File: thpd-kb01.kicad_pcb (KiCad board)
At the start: 2 copper layers, 216 parts, among them SW1 SW_Push, U1 ATmega32U4-AU, Y1 16MHz

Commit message: wip pcb
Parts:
- C1, C2, C3, C4, C5, C6, C7, D1, D10, D100, D11, D12, D13, D14, D15, D16, D17, D18, D19, D2, D20, D21, D22, D23, D24, D25, D26, D27, D28, D29, D3, D30, D31, D32, D33, D34, D35, D36, D37, D38, D39, D4, D40, D41, D42, D43, D44, D45, D46, D47, D48, D49, D5, D50, D51, D52, D53, D54, D55, D56, D57, D58, D59, D6, D60, D61, D62, D63, D64, D65, D66, D67, D68, D69, D7, D70, D71, D72, D73, D74, D75, D76, D77, D78, D79, D8, D80, D81, D82, D83, D84, D85, D86, D87, D88, D89, D9, D90, D91, D92, D93, D94, D95, D96, D97, D98, D99, F1, R1, R2, R3, R4, SW1, U1, USB1, Y1: moved to B.Cu
- moved C2 448.9 mm to (681.0, 19.1)
- moved D89 446.5 mm to (696.9, 39.7), turned to 90 degrees
- moved SW1 445.3 mm to (682.6, 7.94)
- moved R3 441.8 mm to (677.1, 14.3)
- moved U1 438.9 mm to (667.5, 8.73)
- moved R4 435.9 mm to (657.2, 2.38), turned to 270 degrees
- moved C7 434.7 mm to (677.9, -1.59), turned to 180 degrees
- moved C6 431.7 mm to (662.0, -6.35), turned to 270 degrees
- moved C5 430.3 mm to (672.3, -6.35), turned to 90 degrees
- moved Y1 426.9 mm to (666.8, -6.35), turned to 180 degrees
- moved D96 421.3 mm to (677.9, 39.7), turned to 90 degrees
- moved D97 418.5 mm to (677.9, 58.7), turned to 90 degrees
- moved F1 417.6 mm to (631.8, 9.53), turned to 90 degrees
- moved D95 416.4 mm to (689.0, 56.4), turned to 270 degrees
- moved C3 413.1 mm to (656.4, 7.14)
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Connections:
- MX66 pad 1: /keys_matrix/COL11 -> /keys_matrix/COL12

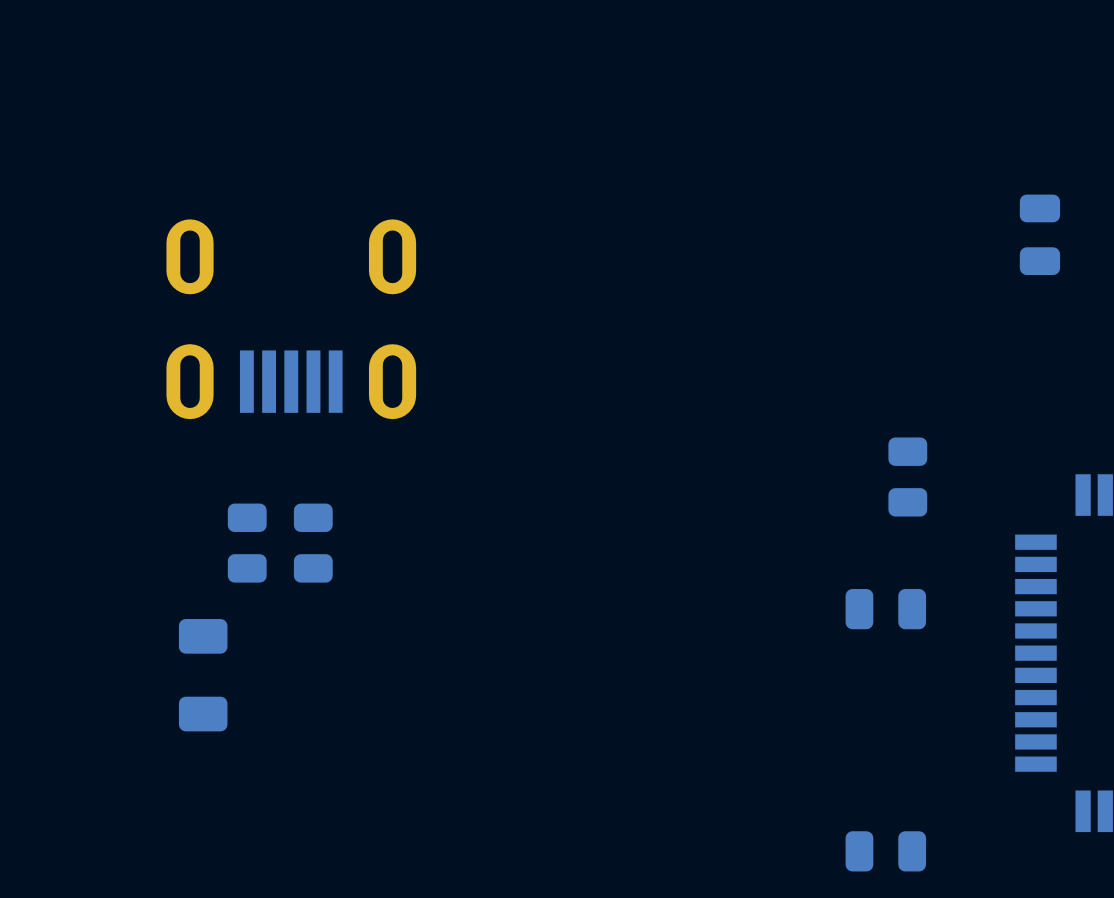
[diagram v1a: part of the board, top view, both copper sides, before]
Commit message: Switch USB B to USB C
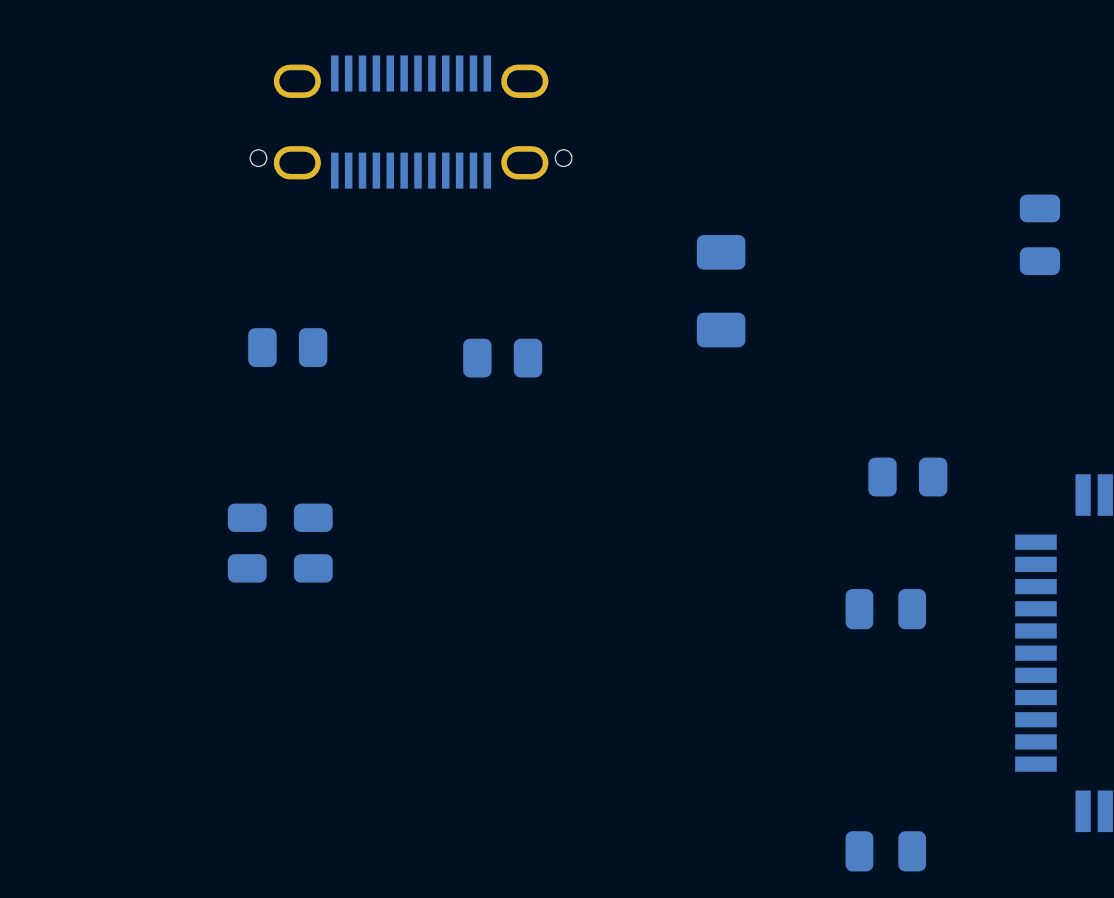
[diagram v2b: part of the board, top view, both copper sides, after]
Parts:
- removed USB1: Molex-0548190589, random-keyboard-parts:Molex-0548190589
- added J1: USB_C_Receptacle_USB2.0, Connector_USB:USB_C_Receptacle_JAE_DX07S024WJ3R400, B.Cu at (639.3, -10.4)
- added R5: 5.1k, Resistor_SMD:R_0805_2012Metric, B.Cu at (634.9, -2.29)
- added R6: 5.1k, Resistor_SMD:R_0805_2012Metric, B.Cu at (642.6, -1.91)
- moved F1 23.2 mm to (650.5, -4.32)
- turned R4 to 0 degrees

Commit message: wip
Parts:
- D1, D10, D100, D11, D12, D13, D14, D15, D16, D17, D18, D19, D2, D20, D21, D22, D23, D24, D25, D26, D27, D28, D29, D3, D30, D31, D32, D33, D34, D35, D36, D37, D38, D39, D4, D40, D41, D42, D43, D44, D45, D46, D47, D48, D49, D5, D50, D51, D52, D53, D54, D55, D56, D57, D58, D59, D6, D60, D61, D62, D63, D64, D65, D66, D67, D68, D69, D7, D70, D71, D72, D73, D74, D75, D76, D77, D78, D79, D8, D80, D81, D82, D83, D84, D85, D86, D87, D88, D89, D9, D90, D91, D92, D93, D94, D95, D96, D97, D98, D99: footprint Diode_SMD:D_SOD-123 -> Diode_SMD:D_SOD-123F
- J1: footprint Connector_USB:USB_C_Receptacle_JAE_DX07S024WJ3R400 -> Connector_USB:USB_C_Receptacle_HRO_TYPE-C-31-M-12
- MX1, MX10, MX11, MX13, MX14, MX15, MX16, MX17, MX19, MX2, MX20, MX21, MX22, MX23, MX24, MX25, MX26, MX27, MX28, MX29, MX30, MX31, MX32, MX33, MX35, MX36, MX37, MX38, MX39, MX40, MX41, MX42, MX43, MX44, MX45, MX46, MX47, MX48, MX49, MX50, MX51, MX52, MX53, MX54, MX55, MX56, MX57, MX58, MX59, MX60, MX61, MX62, MX63, MX64, MX65, MX67, MX68, MX69, MX7, MX70, MX71, MX72, MX75, MX76, MX77, MX78, MX79, MX8, MX80, MX81, MX82, MX83, MX84, MX85, MX86, MX87, MX89, MX9, MX90, MX91, MX92, MX93, MX94, MX96, MX97, MX98, MX99: footprint MX_Alps_Hybrid:MX-1U-NoLED -> Button_Switch_Keyboard:SW_Cherry_MX_1.00u_Plate
- MX100, MX95: footprint MX_Alps_Hybrid:MX-2U-NoLED -> Button_Switch_Keyboard:SW_Cherry_MX_2.00u_Vertical_Plate
- MX12, MX18, MX6: footprint MX_Alps_Hybrid:MX-1.25U-NoLED -> Button_Switch_Keyboard:SW_Cherry_MX_1.25u_Plate
- MX3: footprint MX_Alps_Hybrid:MX-1.5U-NoLED -> Button_Switch_Keyboard:SW_Cherry_MX_1.50u_Plate
- MX34: footprint MX_Alps_Hybrid:MX-6.25U-NoLED -> Button_Switch_Keyboard:SW_Cherry_MX_6.25u_Plate
- MX4, MX66: footprint MX_Alps_Hybrid:MX-1.75U-NoLED -> Button_Switch_Keyboard:SW_Cherry_MX_1.75u_Plate
- MX5: footprint MX_Alps_Hybrid:MX-2.25U-NoLED -> Button_Switch_Keyboard:SW_Cherry_MX_2.25u_Plate
- MX73, MX88: footprint MX_Alps_Hybrid:MX-2U-NoLED -> Button_Switch_Keyboard:SW_Cherry_MX_2.00u_Plate
- MX74: footprint MX_Alps_Hybrid:MX-ISO -> Button_Switch_Keyboard:SW_Cherry_MX_ISOEnter_Plate
- SW1: footprint random-keyboard-parts:SKQG-1155865 -> random-keyboard-parts:SKQGADE010
- moved C6 31.5 mm to (682.6, 17.5)
- moved C5 30.4 mm to (682.6, 22.2), turned to 0 degrees
- moved Y1 28.2 mm to (677.1, 19.8), turned to 270 degrees
- moved J1 22.5 mm to (633.9, 11.4)
- moved R5 22.3 mm to (628.6, 19.2)
- moved F1 20.7 mm to (649.7, 16.3)
- moved R6 19.8 mm to (641.9, 17.9)
- moved C7 16.3 mm to (666.8, 10.3)
- moved R1 16.1 mm to (633.1, 20.8)
- moved R2 16.1 mm to (635.5, 20.8)
- moved SW1 15.7 mm to (696.1, 15.9), turned to 270 degrees
- moved C2 13.5 mm to (670.7, 27.8)
- moved U1 10.3 mm to (666.8, 19.1), turned to 270 degrees
- moved R3 9.66 mm to (686.6, 12.7), turned to 90 degrees
- moved R4 8.59 mm to (662.0, 9.53)
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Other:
- board outline added: 402.4 x 126.2 mm

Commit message: wip
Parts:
- moved D95 15.3 mm to (694.7, 70.6)
- moved D100 12.9 mm to (694.7, 111.3)
- moved D88 7.20 mm to (647.8, 120.6)
- moved SW1 6.40 mm to (692.9, 21.4)
- moved D5 6.32 mm to (341.3, 101.8)
- moved D74 6.22 mm to (593.7, 70.0)
- moved MX91 5.97 mm to (651.0, 59.5)
- moved MX85 5.97 mm to (632.0, 59.5)
- moved C6 5.56 mm to (682.6, 23.0)
- moved R1 5.56 mm to (633.1, 26.4)
- moved R2 5.56 mm to (635.5, 26.4)
- moved R3 5.56 mm to (686.6, 18.3)
- moved R5 5.56 mm to (628.6, 24.7)
- moved C3 5.56 mm to (655.6, 15.9)
- moved C7 5.56 mm to (666.8, 15.9)
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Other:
- board size 402.4 x 126.2 mm -> 390 x 120.6 mm

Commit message: Big changes
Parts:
- removed Y1: 16MHz, Crystal:Crystal_SMD_3225-4Pin_3.2x2.5mm
- added C10: 100nF, Capacitor_SMD:C_0402_1005Metric, F.Cu at (280.1, 71.9)
- added C11: 100nF, Capacitor_SMD:C_0402_1005Metric, F.Cu at (285.2, 67.0)
- added C12: 1uF, Capacitor_SMD:C_0402_1005Metric, F.Cu at (280.1, 69.9)
- added C13: 1uF, Capacitor_SMD:C_0402_1005Metric, F.Cu at (307.0, 42.4)
- added C14: 1uF, Capacitor_SMD:C_0402_1005Metric, F.Cu at (282.0, 67.9)
- added C15: 1uF, Capacitor_SMD:C_0402_1005Metric, F.Cu at (299.8, 53.1)
- added C16: 1uF, Capacitor_SMD:C_0402_1005Metric, F.Cu at (279.1, 67.9)
- added C17: 1uF, Capacitor_SMD:C_0402_1005Metric, F.Cu at (307.0, 40.4)
- added C18: 1uF, Capacitor_SMD:C_0402_1005Metric, F.Cu at (277.2, 71.1)
- added C19: 1uF, Capacitor_SMD:C_0402_1005Metric, F.Cu at (271.5, 70.2)
- added C20: 10nF, Capacitor_SMD:C_0402_1005Metric, F.Cu at (307.0, 48.4)
- added C21: 10nF, Capacitor_SMD:C_0402_1005Metric, F.Cu at (274.3, 71.1)
- added C8: 10nF, Capacitor_SMD:C_0402_1005Metric, F.Cu at (289.2, 64.5)
- added C9: 4.7uF, Capacitor_SMD:C_0402_1005Metric, F.Cu at (307.0, 44.4)
- added D101: D_Small, Diode_SMD:D_SOD-123, B.Cu at (377.8, 191.3)
- added D102: D_Small, Diode_SMD:D_SOD-123, B.Cu at (396.9, 91.3)
- added D103: SK6812, thpd-kb01-custom:LED_SK6812MINI-ER_PLCC4_3.5x2.8mm_P1.8mm, F.Cu at (100.7, 50.7)
- added D104: SK6812, thpd-kb01-custom:LED_SK6812MINI-ER_PLCC4_3.5x2.8mm_P1.8mm, F.Cu at (93.7, 55.7)
- added D105: SK6812, thpd-kb01-custom:LED_SK6812MINI-ER_PLCC4_3.5x2.8mm_P1.8mm, F.Cu at (107.7, 40.6)
- added D106: SK6812, thpd-kb01-custom:LED_SK6812MINI-ER_PLCC4_3.5x2.8mm_P1.8mm, F.Cu at (86.6, 60.8)
- added D107: SK6812, thpd-kb01-custom:LED_SK6812MINI-ER_PLCC4_3.5x2.8mm_P1.8mm, F.Cu at (100.7, 45.6)
- added D108: SK6812, thpd-kb01-custom:LED_SK6812MINI-ER_PLCC4_3.5x2.8mm_P1.8mm, F.Cu at (93.7, 50.7)
- added D109: SK6812, thpd-kb01-custom:LED_SK6812MINI-ER_PLCC4_3.5x2.8mm_P1.8mm, F.Cu at (107.7, 35.5)
- added D110: SK6812, thpd-kb01-custom:LED_SK6812MINI-ER_PLCC4_3.5x2.8mm_P1.8mm, F.Cu at (100.7, 40.6)
- added D111: SK6812, thpd-kb01-custom:LED_SK6812MINI-ER_PLCC4_3.5x2.8mm_P1.8mm, F.Cu at (79.6, 60.8)
- added D112: SK6812, thpd-kb01-custom:LED_SK6812MINI-ER_PLCC4_3.5x2.8mm_P1.8mm, F.Cu at (93.7, 45.6)
- added D113: SK6812, thpd-kb01-custom:LED_SK6812MINI-ER_PLCC4_3.5x2.8mm_P1.8mm, F.Cu at (86.6, 50.7)
- added D114: SK6812, thpd-kb01-custom:LED_SK6812MINI-ER_PLCC4_3.5x2.8mm_P1.8mm, F.Cu at (107.7, 30.5)
- added D115: SK6812, thpd-kb01-custom:LED_SK6812MINI-ER_PLCC4_3.5x2.8mm_P1.8mm, F.Cu at (79.6, 55.7)
- added D116: SK6812, thpd-kb01-custom:LED_SK6812MINI-ER_PLCC4_3.5x2.8mm_P1.8mm, F.Cu at (100.7, 35.5)
- added D117: SK6812, thpd-kb01-custom:LED_SK6812MINI-ER_PLCC4_3.5x2.8mm_P1.8mm, F.Cu at (93.7, 40.6)
- added D118: SK6812, thpd-kb01-custom:LED_SK6812MINI-ER_PLCC4_3.5x2.8mm_P1.8mm, F.Cu at (72.6, 60.8)
- added D119: SK6812, thpd-kb01-custom:LED_SK6812MINI-ER_PLCC4_3.5x2.8mm_P1.8mm, F.Cu at (86.6, 45.6)
- added D120: SK6812, thpd-kb01-custom:LED_SK6812MINI-ER_PLCC4_3.5x2.8mm_P1.8mm, F.Cu at (107.7, 25.4)
- added D121: SK6812, thpd-kb01-custom:LED_SK6812MINI-ER_PLCC4_3.5x2.8mm_P1.8mm, F.Cu at (79.6, 50.7)
- added D122: SK6812, thpd-kb01-custom:LED_SK6812MINI-ER_PLCC4_3.5x2.8mm_P1.8mm, F.Cu at (100.7, 30.5)
- added D123: SK6812, thpd-kb01-custom:LED_SK6812MINI-ER_PLCC4_3.5x2.8mm_P1.8mm, F.Cu at (72.6, 55.7)
- added D124: SK6812, thpd-kb01-custom:LED_SK6812MINI-ER_PLCC4_3.5x2.8mm_P1.8mm, F.Cu at (93.7, 35.5)
- added D125: SK6812, thpd-kb01-custom:LED_SK6812MINI-ER_PLCC4_3.5x2.8mm_P1.8mm, F.Cu at (86.6, 40.6)
- added D126: SK6812, thpd-kb01-custom:LED_SK6812MINI-ER_PLCC4_3.5x2.8mm_P1.8mm, F.Cu at (65.6, 60.8)
- added D127: SK6812, thpd-kb01-custom:LED_SK6812MINI-ER_PLCC4_3.5x2.8mm_P1.8mm, F.Cu at (107.7, 20.4)
- added D128: SK6812, thpd-kb01-custom:LED_SK6812MINI-ER_PLCC4_3.5x2.8mm_P1.8mm, F.Cu at (79.6, 45.6)
- added D129: SK6812, thpd-kb01-custom:LED_SK6812MINI-ER_PLCC4_3.5x2.8mm_P1.8mm, F.Cu at (100.7, 25.4)
- added D130: SK6812, thpd-kb01-custom:LED_SK6812MINI-ER_PLCC4_3.5x2.8mm_P1.8mm, F.Cu at (72.6, 50.7)
- added D131: SK6812, thpd-kb01-custom:LED_SK6812MINI-ER_PLCC4_3.5x2.8mm_P1.8mm, F.Cu at (93.7, 30.5)
- added D132: SK6812, thpd-kb01-custom:LED_SK6812MINI-ER_PLCC4_3.5x2.8mm_P1.8mm, F.Cu at (65.6, 55.7)
- added D133: SK6812, thpd-kb01-custom:LED_SK6812MINI-ER_PLCC4_3.5x2.8mm_P1.8mm, F.Cu at (86.6, 35.5)
- added D134: SK6812, thpd-kb01-custom:LED_SK6812MINI-ER_PLCC4_3.5x2.8mm_P1.8mm, F.Cu at (79.6, 40.6)
- added D135: SK6812, thpd-kb01-custom:LED_SK6812MINI-ER_PLCC4_3.5x2.8mm_P1.8mm, F.Cu at (58.6, 60.8)
- added D136: SK6812, thpd-kb01-custom:LED_SK6812MINI-ER_PLCC4_3.5x2.8mm_P1.8mm, F.Cu at (100.7, 20.4)
- added D137: SK6812, thpd-kb01-custom:LED_SK6812MINI-ER_PLCC4_3.5x2.8mm_P1.8mm, F.Cu at (72.6, 45.6)
- added D138: SK6812, thpd-kb01-custom:LED_SK6812MINI-ER_PLCC4_3.5x2.8mm_P1.8mm, F.Cu at (93.7, 25.4)
- added D139: SK6812, thpd-kb01-custom:LED_SK6812MINI-ER_PLCC4_3.5x2.8mm_P1.8mm, F.Cu at (65.6, 50.7)
- added D140: SK6812, thpd-kb01-custom:LED_SK6812MINI-ER_PLCC4_3.5x2.8mm_P1.8mm, F.Cu at (86.6, 30.5)
- added D141: SK6812, thpd-kb01-custom:LED_SK6812MINI-ER_PLCC4_3.5x2.8mm_P1.8mm, F.Cu at (58.6, 55.7)
- added D142: SK6812, thpd-kb01-custom:LED_SK6812MINI-ER_PLCC4_3.5x2.8mm_P1.8mm, F.Cu at (79.6, 35.5)
- added D143: SK6812, thpd-kb01-custom:LED_SK6812MINI-ER_PLCC4_3.5x2.8mm_P1.8mm, F.Cu at (72.6, 40.6)
- added D144: SK6812, thpd-kb01-custom:LED_SK6812MINI-ER_PLCC4_3.5x2.8mm_P1.8mm, F.Cu at (51.5, 60.8)
- added D145: SK6812, thpd-kb01-custom:LED_SK6812MINI-ER_PLCC4_3.5x2.8mm_P1.8mm, F.Cu at (93.7, 20.4)
- added D146: SK6812, thpd-kb01-custom:LED_SK6812MINI-ER_PLCC4_3.5x2.8mm_P1.8mm, F.Cu at (65.6, 45.6)
- added D147: SK6812, thpd-kb01-custom:LED_SK6812MINI-ER_PLCC4_3.5x2.8mm_P1.8mm, F.Cu at (86.6, 25.4)
- added D148: SK6812, thpd-kb01-custom:LED_SK6812MINI-ER_PLCC4_3.5x2.8mm_P1.8mm, F.Cu at (58.6, 50.7)
- added D149: SK6812, thpd-kb01-custom:LED_SK6812MINI-ER_PLCC4_3.5x2.8mm_P1.8mm, F.Cu at (79.6, 30.5)
- added D150: SK6812, thpd-kb01-custom:LED_SK6812MINI-ER_PLCC4_3.5x2.8mm_P1.8mm, F.Cu at (51.5, 55.7)
- added D151: SK6812, thpd-kb01-custom:LED_SK6812MINI-ER_PLCC4_3.5x2.8mm_P1.8mm, F.Cu at (72.6, 35.5)
- added D152: SK6812, thpd-kb01-custom:LED_SK6812MINI-ER_PLCC4_3.5x2.8mm_P1.8mm, F.Cu at (86.6, 55.7)
- added D153: SK6812, thpd-kb01-custom:LED_SK6812MINI-ER_PLCC4_3.5x2.8mm_P1.8mm, F.Cu at (65.6, 40.6)
- added D154: SK6812, thpd-kb01-custom:LED_SK6812MINI-ER_PLCC4_3.5x2.8mm_P1.8mm, F.Cu at (44.5, 60.8)
- added D155: SK6812, thpd-kb01-custom:LED_SK6812MINI-ER_PLCC4_3.5x2.8mm_P1.8mm, F.Cu at (86.6, 20.4)
- added D156: SK6812, thpd-kb01-custom:LED_SK6812MINI-ER_PLCC4_3.5x2.8mm_P1.8mm, F.Cu at (58.6, 45.6)
- added D157: SK6812, thpd-kb01-custom:LED_SK6812MINI-ER_PLCC4_3.5x2.8mm_P1.8mm, F.Cu at (79.6, 25.4)
- added D158: SK6812, thpd-kb01-custom:LED_SK6812MINI-ER_PLCC4_3.5x2.8mm_P1.8mm, F.Cu at (51.5, 50.7)
- added D159: SK6812, thpd-kb01-custom:LED_SK6812MINI-ER_PLCC4_3.5x2.8mm_P1.8mm, F.Cu at (72.6, 30.5)
- added D160: SK6812, thpd-kb01-custom:LED_SK6812MINI-ER_PLCC4_3.5x2.8mm_P1.8mm, F.Cu at (44.5, 55.7)
- added D161: SK6812, thpd-kb01-custom:LED_SK6812MINI-ER_PLCC4_3.5x2.8mm_P1.8mm, F.Cu at (65.6, 35.5)
- added D162: SK6812, thpd-kb01-custom:LED_SK6812MINI-ER_PLCC4_3.5x2.8mm_P1.8mm, F.Cu at (58.6, 40.6)
- added D163: SK6812, thpd-kb01-custom:LED_SK6812MINI-ER_PLCC4_3.5x2.8mm_P1.8mm, F.Cu at (37.5, 60.8)
- added D164: SK6812, thpd-kb01-custom:LED_SK6812MINI-ER_PLCC4_3.5x2.8mm_P1.8mm, F.Cu at (79.6, 20.4)
- added D165: SK6812, thpd-kb01-custom:LED_SK6812MINI-ER_PLCC4_3.5x2.8mm_P1.8mm, F.Cu at (51.5, 45.6)
- added D166: SK6812, thpd-kb01-custom:LED_SK6812MINI-ER_PLCC4_3.5x2.8mm_P1.8mm, F.Cu at (72.6, 25.4)
- added D167: SK6812, thpd-kb01-custom:LED_SK6812MINI-ER_PLCC4_3.5x2.8mm_P1.8mm, F.Cu at (44.5, 50.7)
- added D168: SK6812, thpd-kb01-custom:LED_SK6812MINI-ER_PLCC4_3.5x2.8mm_P1.8mm, F.Cu at (65.6, 30.5)
- added D169: SK6812, thpd-kb01-custom:LED_SK6812MINI-ER_PLCC4_3.5x2.8mm_P1.8mm, F.Cu at (37.5, 55.7)
- added D170: SK6812, thpd-kb01-custom:LED_SK6812MINI-ER_PLCC4_3.5x2.8mm_P1.8mm, F.Cu at (58.6, 35.5)
- added D171: SK6812, thpd-kb01-custom:LED_SK6812MINI-ER_PLCC4_3.5x2.8mm_P1.8mm, F.Cu at (51.5, 40.6)
- added D172: SK6812, thpd-kb01-custom:LED_SK6812MINI-ER_PLCC4_3.5x2.8mm_P1.8mm, F.Cu at (30.5, 60.8)
- added D173: SK6812, thpd-kb01-custom:LED_SK6812MINI-ER_PLCC4_3.5x2.8mm_P1.8mm, F.Cu at (72.6, 20.4)
- added D174: SK6812, thpd-kb01-custom:LED_SK6812MINI-ER_PLCC4_3.5x2.8mm_P1.8mm, F.Cu at (44.5, 45.6)
- added D175: SK6812, thpd-kb01-custom:LED_SK6812MINI-ER_PLCC4_3.5x2.8mm_P1.8mm, F.Cu at (65.6, 25.4)
- added D176: SK6812, thpd-kb01-custom:LED_SK6812MINI-ER_PLCC4_3.5x2.8mm_P1.8mm, F.Cu at (37.5, 50.7)
- added D177: SK6812, thpd-kb01-custom:LED_SK6812MINI-ER_PLCC4_3.5x2.8mm_P1.8mm, F.Cu at (58.6, 30.5)
- added D178: SK6812, thpd-kb01-custom:LED_SK6812MINI-ER_PLCC4_3.5x2.8mm_P1.8mm, F.Cu at (30.5, 55.7)
- added D179: SK6812, thpd-kb01-custom:LED_SK6812MINI-ER_PLCC4_3.5x2.8mm_P1.8mm, F.Cu at (51.5, 35.5)
- added D180: SK6812, thpd-kb01-custom:LED_SK6812MINI-ER_PLCC4_3.5x2.8mm_P1.8mm, F.Cu at (44.5, 40.6)
- added D181: SK6812, thpd-kb01-custom:LED_SK6812MINI-ER_PLCC4_3.5x2.8mm_P1.8mm, F.Cu at (65.6, 20.4)
- added D182: SK6812, thpd-kb01-custom:LED_SK6812MINI-ER_PLCC4_3.5x2.8mm_P1.8mm, F.Cu at (37.5, 45.6)
- added D183: SK6812, thpd-kb01-custom:LED_SK6812MINI-ER_PLCC4_3.5x2.8mm_P1.8mm, F.Cu at (58.6, 25.4)
- added D184: SK6812, thpd-kb01-custom:LED_SK6812MINI-ER_PLCC4_3.5x2.8mm_P1.8mm, F.Cu at (30.5, 50.7)
- added D185: SK6812, thpd-kb01-custom:LED_SK6812MINI-ER_PLCC4_3.5x2.8mm_P1.8mm, F.Cu at (51.5, 30.5)
- added D186: SK6812, thpd-kb01-custom:LED_SK6812MINI-ER_PLCC4_3.5x2.8mm_P1.8mm, F.Cu at (44.5, 35.5)
- added D187: SK6812, thpd-kb01-custom:LED_SK6812MINI-ER_PLCC4_3.5x2.8mm_P1.8mm, F.Cu at (37.5, 40.6)
- added D188: SK6812, thpd-kb01-custom:LED_SK6812MINI-ER_PLCC4_3.5x2.8mm_P1.8mm, F.Cu at (58.6, 20.4)
- added D189: SK6812, thpd-kb01-custom:LED_SK6812MINI-ER_PLCC4_3.5x2.8mm_P1.8mm, F.Cu at (30.5, 45.6)
- added D190: SK6812, thpd-kb01-custom:LED_SK6812MINI-ER_PLCC4_3.5x2.8mm_P1.8mm, F.Cu at (51.5, 25.4)
- added D191: SK6812, thpd-kb01-custom:LED_SK6812MINI-ER_PLCC4_3.5x2.8mm_P1.8mm, F.Cu at (44.5, 30.5)
- added D192: SK6812, thpd-kb01-custom:LED_SK6812MINI-ER_PLCC4_3.5x2.8mm_P1.8mm, F.Cu at (37.5, 35.5)
- added D193: SK6812, thpd-kb01-custom:LED_SK6812MINI-ER_PLCC4_3.5x2.8mm_P1.8mm, F.Cu at (30.5, 40.6)
- added D194: SK6812, thpd-kb01-custom:LED_SK6812MINI-ER_PLCC4_3.5x2.8mm_P1.8mm, F.Cu at (51.5, 20.4)
- added D195: SK6812, thpd-kb01-custom:LED_SK6812MINI-ER_PLCC4_3.5x2.8mm_P1.8mm, F.Cu at (44.5, 25.4)
- added D196: SK6812, thpd-kb01-custom:LED_SK6812MINI-ER_PLCC4_3.5x2.8mm_P1.8mm, F.Cu at (37.5, 30.5)
- added D197: SK6812, thpd-kb01-custom:LED_SK6812MINI-ER_PLCC4_3.5x2.8mm_P1.8mm, F.Cu at (30.5, 35.5)
- added D198: SK6812, thpd-kb01-custom:LED_SK6812MINI-ER_PLCC4_3.5x2.8mm_P1.8mm, F.Cu at (44.5, 20.4)
- added D199: SK6812, thpd-kb01-custom:LED_SK6812MINI-ER_PLCC4_3.5x2.8mm_P1.8mm, F.Cu at (37.5, 25.4)
- added D200: SK6812, thpd-kb01-custom:LED_SK6812MINI-ER_PLCC4_3.5x2.8mm_P1.8mm, F.Cu at (30.5, 30.5)
- added D201: SK6812, thpd-kb01-custom:LED_SK6812MINI-ER_PLCC4_3.5x2.8mm_P1.8mm, F.Cu at (37.5, 20.4)
- added D202: SK6812, thpd-kb01-custom:LED_SK6812MINI-ER_PLCC4_3.5x2.8mm_P1.8mm, F.Cu at (30.5, 25.4)
- added D203: SK6812, thpd-kb01-custom:LED_SK6812MINI-ER_PLCC4_3.5x2.8mm_P1.8mm, F.Cu at (30.5, 20.4)
- added MX101: Num., Button_Switch_Keyboard:SW_Cherry_MX_1.00u_Plate, F.Cu at (377.0, 181.8)
- added R10: 500, Resistor_SMD:R_0402_1005Metric, F.Cu at (24.6, 67.5)
- added R7: 10k, Resistor_SMD:R_0603_1608Metric, F.Cu at (258.2, 70.6)
- added R8: 10k, Resistor_SMD:R_0603_1608Metric, F.Cu at (285.7, 64.7)
- added R9: 10k, Resistor_SMD:R_0603_1608Metric, F.Cu at (262.2, 70.6)
- added SW2: SW_SPDT, thpd-kb01-custom:SW_SPDT_K3-1296S-E1, F.Cu at (261.4, 65.6)
- added SW3: Rotary_Encoder_Switch, Rotary_Encoder:RotaryEncoder_Alps_EC11E-Switch_Vertical_H20mm, F.Cu at (377.0, 85.7)
- added U2: USBLC6-2SC6, Package_TO_SOT_SMD:SOT-23-6, F.Cu at (281.3, 64.6)
- added U3: NHD-C12832A1Z, thpd-kb01-custom:NHD-C12832A1Z, F.Cu at (351.6, 88.1)
- added U4: STM32F072C8Tx, Package_QFP:LQFP-48_7x7mm_P0.5mm, F.Cu at (292.7, 57.8)
- C1, C2: value 0.1uF -> 1uF; footprint Capacitor_SMD:C_0805_2012Metric -> Capacitor_SMD:C_0402_1005Metric; moved to F.Cu
- C3: value 0.1uF -> 4.7uF; footprint Capacitor_SMD:C_0805_2012Metric -> Capacitor_SMD:C_0402_1005Metric; moved to F.Cu
- C4: value 10uF -> 100nF; footprint Capacitor_SMD:C_0805_2012Metric -> Capacitor_SMD:C_0402_1005Metric; moved to F.Cu
- C5, C6: value 22pF -> 100nF; footprint Capacitor_SMD:C_0805_2012Metric -> Capacitor_SMD:C_0402_1005Metric; moved to F.Cu
- C7: footprint Capacitor_SMD:C_0805_2012Metric -> Capacitor_SMD:C_0402_1005Metric; moved to F.Cu
- D1, D10, D100, D11, D12, D13, D14, D15, D16, D17, D18, D19, D2, D20, D21, D22, D23, D24, D25, D26, D27, D28, D29, D3, D30, D31, D32, D33, D34, D35, D36, D37, D38, D39, D4, D40, D41, D42, D43, D44, D45, D46, D47, D48, D49, D5, D50, D51, D52, D53, D54, D55, D56, D57, D58, D59, D6, D60, D61, D62, D63, D64, D65, D66, D67, D68, D69, D7, D70, D71, D72, D73, D74, D75, D76, D77, D78, D79, D8, D80, D81, D82, D83, D84, D85, D86, D87, D88, D89, D9, D90, D91, D92, D93, D94, D95, D96, D97, D98, D99: footprint Diode_SMD:D_SOD-123F -> Diode_SMD:D_SOD-123
- F1, J1: moved to F.Cu
- MX10: value A -> F9
- MX100: value NumEnter -> Num0; footprint Button_Switch_Keyboard:SW_Cherry_MX_2.00u_Vertical_Plate -> Button_Switch_Keyboard:SW_Cherry_MX_2.00u_Plate
- MX11: value Z -> F10
- MX12: value Win -> F11; footprint Button_Switch_Keyboard:SW_Cherry_MX_1.25u_Plate -> Button_Switch_Keyboard:SW_Cherry_MX_1.00u_Plate
- MX13: value F2 -> F12
- MX14: value 2 -> F13
- MX15: value W -> F14
- MX16: value S -> Delete
- MX17: value X -> Tilde/Backtick
- MX18: value Alt -> 1; footprint Button_Switch_Keyboard:SW_Cherry_MX_1.25u_Plate -> Button_Switch_Keyboard:SW_Cherry_MX_1.00u_Plate
- MX19: value F3 -> 2
- MX2: value ~` -> F1
- MX21: value E -> 4
- MX22: value D -> 5
- MX23: value C -> 6
- MX24: value F4 -> 7
- MX25: value 4 -> 8
- MX26: value R -> 9
- MX27: value F -> 0
- MX28: value V -> Hyphen
- MX29: value F5 -> Equals
- MX3: value Tab -> F2; footprint Button_Switch_Keyboard:SW_Cherry_MX_1.50u_Plate -> Button_Switch_Keyboard:SW_Cherry_MX_1.00u_Plate
- MX30: value 5 -> Backspace; footprint Button_Switch_Keyboard:SW_Cherry_MX_1.00u_Plate -> Button_Switch_Keyboard:SW_Cherry_MX_2.00u_Plate
- MX31: value T -> Home
- MX32: value G -> NumLock
- MX33: value B -> Num/
- MX34: value Spacebar -> Num*; footprint Button_Switch_Keyboard:SW_Cherry_MX_6.25u_Plate -> Button_Switch_Keyboard:SW_Cherry_MX_1.00u_Plate
- MX35: value F6 -> Num-
- MX36: value 6 -> Tab; footprint Button_Switch_Keyboard:SW_Cherry_MX_1.00u_Plate -> Button_Switch_Keyboard:SW_Cherry_MX_1.50u_Plate
- MX37: value Y -> Q
- MX38: value H -> W
- MX39: value N -> E
- MX4: value Caps Lock -> F3; footprint Button_Switch_Keyboard:SW_Cherry_MX_1.75u_Plate -> Button_Switch_Keyboard:SW_Cherry_MX_1.00u_Plate
- MX40: value F7 -> R
- MX41: value 7 -> T
- MX42: value U -> Y
- MX43: value J -> U
- MX44: value M -> I
- MX45: value F8 -> O
- MX46: value 8 -> P
- MX47: value I -> {
- MX48: value K -> }
- MX49: value < -> Enter; footprint Button_Switch_Keyboard:SW_Cherry_MX_1.00u_Plate -> Button_Switch_Keyboard:SW_Cherry_MX_ISOEnter_Plate
- MX5: value Shift -> F4; footprint Button_Switch_Keyboard:SW_Cherry_MX_2.25u_Plate -> Button_Switch_Keyboard:SW_Cherry_MX_1.00u_Plate
- MX50: value F9 -> PageUp
- MX51: value 9 -> Num7
- MX52: value O -> Num8
- MX53: value L -> Num9
- MX54: value > -> Num+; footprint Button_Switch_Keyboard:SW_Cherry_MX_1.00u_Plate -> Button_Switch_Keyboard:SW_Cherry_MX_2.00u_Vertical_Plate
- MX55: value RAlt -> Caps Lock; footprint Button_Switch_Keyboard:SW_Cherry_MX_1.00u_Plate -> Button_Switch_Keyboard:SW_Cherry_MX_1.75u_Plate
- MX56: value F10 -> A
- MX57: value 0 -> S
- MX58: value P -> D
- MX59: value ; -> F
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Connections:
- C1 pad 1: +5V -> Net-(C1-Pad1)
- C2 pad 1: +5V -> +3V3
- C3 pad 1: +5V -> +3V3
- C4 pad 1: +5V -> +3V3
- C5 pad 1: Net-(C5-Pad1) -> +3V3
- C6 pad 1: Net-(C6-Pad1) -> +3V3
- C7 pad 1: Net-(C7-Pad1) -> +3V3
- D10 pad 1: /keys_matrix/ROW3 -> /keys_matrix/ROW0
- D11 pad 1: /keys_matrix/ROW4 -> /keys_matrix/ROW0
- D12 pad 1: /keys_matrix/ROW5 -> /keys_matrix/ROW0
- D14 pad 1: /keys_matrix/ROW1 -> /keys_matrix/ROW0
- D15 pad 1: /keys_matrix/ROW2 -> /keys_matrix/ROW0
- D16 pad 1: /keys_matrix/ROW3 -> /keys_matrix/ROW0
- D17 pad 1: /keys_matrix/ROW4 -> /keys_matrix/ROW0
- D17 pad 2: Net-(D17-Pad2) -> ROT_SW_ROW
- D18 pad 1: /keys_matrix/ROW5 -> /keys_matrix/ROW1
- D19 pad 1: /keys_matrix/ROW0 -> /keys_matrix/ROW1
- D2 pad 1: /keys_matrix/ROW1 -> /keys_matrix/ROW0
- D21 pad 1: /keys_matrix/ROW2 -> /keys_matrix/ROW1
- D22 pad 1: /keys_matrix/ROW3 -> /keys_matrix/ROW1
- D23 pad 1: /keys_matrix/ROW4 -> /keys_matrix/ROW1
- D24 pad 1: /keys_matrix/ROW0 -> /keys_matrix/ROW1
- D26 pad 1: /keys_matrix/ROW2 -> /keys_matrix/ROW1
- D27 pad 1: /keys_matrix/ROW3 -> /keys_matrix/ROW1
- D28 pad 1: /keys_matrix/ROW4 -> /keys_matrix/ROW1
- D29 pad 1: /keys_matrix/ROW0 -> /keys_matrix/ROW1
- D3 pad 1: /keys_matrix/ROW2 -> /keys_matrix/ROW0
- D31 pad 1: /keys_matrix/ROW2 -> /keys_matrix/ROW1
- D32 pad 1: /keys_matrix/ROW3 -> /keys_matrix/ROW1
- D33 pad 1: /keys_matrix/ROW4 -> /keys_matrix/ROW1
- D34 pad 1: /keys_matrix/ROW5 -> /keys_matrix/ROW1
- D35 pad 1: /keys_matrix/ROW0 -> /keys_matrix/ROW1
- D38 pad 1: /keys_matrix/ROW3 -> /keys_matrix/ROW2
- D39 pad 1: /keys_matrix/ROW4 -> /keys_matrix/ROW2
- D4 pad 1: /keys_matrix/ROW3 -> /keys_matrix/ROW0
- D40 pad 1: /keys_matrix/ROW0 -> /keys_matrix/ROW2
- D41 pad 1: /keys_matrix/ROW1 -> /keys_matrix/ROW2
- D43 pad 1: /keys_matrix/ROW3 -> /keys_matrix/ROW2
- D44 pad 1: /keys_matrix/ROW4 -> /keys_matrix/ROW2
- D45 pad 1: /keys_matrix/ROW0 -> /keys_matrix/ROW2
- D46 pad 1: /keys_matrix/ROW1 -> /keys_matrix/ROW2
- D48 pad 1: /keys_matrix/ROW3 -> /keys_matrix/ROW2
- D49 pad 1: /keys_matrix/ROW4 -> /keys_matrix/ROW2
- D5 pad 1: /keys_matrix/ROW4 -> /keys_matrix/ROW0
- D50 pad 1: /keys_matrix/ROW0 -> /keys_matrix/ROW2
- D51 pad 1: /keys_matrix/ROW1 -> /keys_matrix/ROW2
- D53 pad 1: /keys_matrix/ROW3 -> /keys_matrix/ROW2
- D54 pad 1: /keys_matrix/ROW4 -> /keys_matrix/ROW2
- D55 pad 1: /keys_matrix/ROW5 -> /keys_matrix/ROW2
- D56 pad 1: /keys_matrix/ROW0 -> /keys_matrix/ROW3
- D57 pad 1: /keys_matrix/ROW1 -> /keys_matrix/ROW3
- D58 pad 1: /keys_matrix/ROW2 -> /keys_matrix/ROW3
- D6 pad 1: /keys_matrix/ROW5 -> /keys_matrix/ROW0
- D60 pad 1: /keys_matrix/ROW4 -> /keys_matrix/ROW3
- D61 pad 1: /keys_matrix/ROW5 -> /keys_matrix/ROW3
- D62 pad 1: /keys_matrix/ROW0 -> /keys_matrix/ROW3
- D63 pad 1: /keys_matrix/ROW1 -> /keys_matrix/ROW3
- D64 pad 1: /keys_matrix/ROW2 -> /keys_matrix/ROW3
- D66 pad 1: /keys_matrix/ROW4 -> /keys_matrix/ROW3
- D67 pad 1: /keys_matrix/ROW5 -> /keys_matrix/ROW3
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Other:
- board outline removed
- copper layers 2 -> 4

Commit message: WIP
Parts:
- removed D104, D113, D114, D115, D116, D117, D118, D119, D120, D121, D122, D123, D124, D125, D126, D127, D128, D129, D130, D131, D132, D133, D134, D135, D136, D137, D138, D139, D140, D141, D142, D143, D144, D145, D146, D147, D148, D149, D150, D151, D152, D153, D154, D155, D156, D157, D158, D159, D160, D161, D162, D163, D164, D165, D166, D167, D168, D169, D170, D171, D172, D173, D174, D175, D176, D177, D178, D179, D180, D181, D182, D183, D184, D185, D186, D187, D188, D189, D190, D191, D192, D193, D194, D195, D196, D197, D198, D199, D200, D201, D202, D203: SK6812, thpd-kb01-custom:LED_SK6812MINI-ER_PLCC4_3.5x2.8mm_P1.8mm
- added LED100: SK6812, thpd-kb01-custom:LED_SK6812MINI-ER_PLCC4_3.5x2.8mm_P1.8mm, F.Cu at (346.1, 191.3)
- added LED101: SK6812, thpd-kb01-custom:LED_SK6812MINI-ER_PLCC4_3.5x2.8mm_P1.8mm, F.Cu at (374.6, 191.3)
- added LED11: SK6812, thpd-kb01-custom:LED_SK6812MINI-ER_PLCC4_3.5x2.8mm_P1.8mm, F.Cu at (217.5, 96.0)
- added LED12: SK6812, thpd-kb01-custom:LED_SK6812MINI-ER_PLCC4_3.5x2.8mm_P1.8mm, F.Cu at (236.5, 96.0)
- added LED13: SK6812, thpd-kb01-custom:LED_SK6812MINI-ER_PLCC4_3.5x2.8mm_P1.8mm, F.Cu at (255.6, 96.0)
- added LED14: SK6812, thpd-kb01-custom:LED_SK6812MINI-ER_PLCC4_3.5x2.8mm_P1.8mm, F.Cu at (274.6, 96.0)
- added LED15: SK6812, thpd-kb01-custom:LED_SK6812MINI-ER_PLCC4_3.5x2.8mm_P1.8mm, F.Cu at (293.7, 96.0)
- added LED16: SK6812, thpd-kb01-custom:LED_SK6812MINI-ER_PLCC4_3.5x2.8mm_P1.8mm, F.Cu at (312.7, 96.0)
- added LED17: SK6812, thpd-kb01-custom:LED_SK6812MINI-ER_PLCC4_3.5x2.8mm_P1.8mm, F.Cu at (27.0, 115.1)
- added LED18: SK6812, thpd-kb01-custom:LED_SK6812MINI-ER_PLCC4_3.5x2.8mm_P1.8mm, F.Cu at (46.0, 115.1)
- added LED19: SK6812, thpd-kb01-custom:LED_SK6812MINI-ER_PLCC4_3.5x2.8mm_P1.8mm, F.Cu at (65.1, 115.1)
- added LED2: SK6812, thpd-kb01-custom:LED_SK6812MINI-ER_PLCC4_3.5x2.8mm_P1.8mm, F.Cu at (45.9, 96.0)
- added LED20: SK6812, thpd-kb01-custom:LED_SK6812MINI-ER_PLCC4_3.5x2.8mm_P1.8mm, F.Cu at (84.1, 115.1)
- added LED21: SK6812, thpd-kb01-custom:LED_SK6812MINI-ER_PLCC4_3.5x2.8mm_P1.8mm, F.Cu at (103.2, 115.1)
- added LED22: SK6812, thpd-kb01-custom:LED_SK6812MINI-ER_PLCC4_3.5x2.8mm_P1.8mm, F.Cu at (122.2, 115.1)
- added LED23: SK6812, thpd-kb01-custom:LED_SK6812MINI-ER_PLCC4_3.5x2.8mm_P1.8mm, F.Cu at (141.3, 115.1)
- added LED24: SK6812, thpd-kb01-custom:LED_SK6812MINI-ER_PLCC4_3.5x2.8mm_P1.8mm, F.Cu at (160.3, 115.1)
- added LED25: SK6812, thpd-kb01-custom:LED_SK6812MINI-ER_PLCC4_3.5x2.8mm_P1.8mm, F.Cu at (179.4, 115.1)
- added LED26: SK6812, thpd-kb01-custom:LED_SK6812MINI-ER_PLCC4_3.5x2.8mm_P1.8mm, F.Cu at (198.4, 115.1)
- added LED27: SK6812, thpd-kb01-custom:LED_SK6812MINI-ER_PLCC4_3.5x2.8mm_P1.8mm, F.Cu at (217.5, 115.1)
- added LED28: SK6812, thpd-kb01-custom:LED_SK6812MINI-ER_PLCC4_3.5x2.8mm_P1.8mm, F.Cu at (236.5, 115.1)
- added LED29: SK6812, thpd-kb01-custom:LED_SK6812MINI-ER_PLCC4_3.5x2.8mm_P1.8mm, F.Cu at (255.6, 115.1)
- added LED30: SK6812, thpd-kb01-custom:LED_SK6812MINI-ER_PLCC4_3.5x2.8mm_P1.8mm, F.Cu at (284.2, 115.1)
- added LED31: SK6812, thpd-kb01-custom:LED_SK6812MINI-ER_PLCC4_3.5x2.8mm_P1.8mm, F.Cu at (312.7, 115.1)
- added LED32: SK6812, thpd-kb01-custom:LED_SK6812MINI-ER_PLCC4_3.5x2.8mm_P1.8mm, F.Cu at (336.6, 115.1)
- added LED33: SK6812, thpd-kb01-custom:LED_SK6812MINI-ER_PLCC4_3.5x2.8mm_P1.8mm, F.Cu at (355.6, 115.1)
- added LED34: SK6812, thpd-kb01-custom:LED_SK6812MINI-ER_PLCC4_3.5x2.8mm_P1.8mm, F.Cu at (374.6, 115.1)
- added LED35: SK6812, thpd-kb01-custom:LED_SK6812MINI-ER_PLCC4_3.5x2.8mm_P1.8mm, F.Cu at (393.7, 115.1)
- added LED36: SK6812, thpd-kb01-custom:LED_SK6812MINI-ER_PLCC4_3.5x2.8mm_P1.8mm, F.Cu at (31.8, 134.1)
- added LED37: SK6812, thpd-kb01-custom:LED_SK6812MINI-ER_PLCC4_3.5x2.8mm_P1.8mm, F.Cu at (55.6, 134.1)
- added LED38: SK6812, thpd-kb01-custom:LED_SK6812MINI-ER_PLCC4_3.5x2.8mm_P1.8mm, F.Cu at (74.6, 134.1)
- added LED39: SK6812, thpd-kb01-custom:LED_SK6812MINI-ER_PLCC4_3.5x2.8mm_P1.8mm, F.Cu at (93.7, 134.1)
- added LED40: SK6812, thpd-kb01-custom:LED_SK6812MINI-ER_PLCC4_3.5x2.8mm_P1.8mm, F.Cu at (112.7, 134.1)
- added LED41: SK6812, thpd-kb01-custom:LED_SK6812MINI-ER_PLCC4_3.5x2.8mm_P1.8mm, F.Cu at (131.8, 134.1)
- added LED42: SK6812, thpd-kb01-custom:LED_SK6812MINI-ER_PLCC4_3.5x2.8mm_P1.8mm, F.Cu at (150.8, 134.1)
- added LED43: SK6812, thpd-kb01-custom:LED_SK6812MINI-ER_PLCC4_3.5x2.8mm_P1.8mm, F.Cu at (169.9, 134.1)
- added LED44: SK6812, thpd-kb01-custom:LED_SK6812MINI-ER_PLCC4_3.5x2.8mm_P1.8mm, F.Cu at (188.9, 134.1)
- added LED45: SK6812, thpd-kb01-custom:LED_SK6812MINI-ER_PLCC4_3.5x2.8mm_P1.8mm, F.Cu at (208.0, 134.1)
- added LED46: SK6812, thpd-kb01-custom:LED_SK6812MINI-ER_PLCC4_3.5x2.8mm_P1.8mm, F.Cu at (227.0, 134.1)
- added LED47: SK6812, thpd-kb01-custom:LED_SK6812MINI-ER_PLCC4_3.5x2.8mm_P1.8mm, F.Cu at (246.1, 134.1)
- added LED48: SK6812, thpd-kb01-custom:LED_SK6812MINI-ER_PLCC4_3.5x2.8mm_P1.8mm, F.Cu at (265.1, 134.1)
- added LED49: SK6812, thpd-kb01-custom:LED_SK6812MINI-ER_PLCC4_3.5x2.8mm_P1.8mm, F.Cu at (291.3, 143.7)
- added LED50: SK6812, thpd-kb01-custom:LED_SK6812MINI-ER_PLCC4_3.5x2.8mm_P1.8mm, F.Cu at (312.7, 134.1)
- added LED51: SK6812, thpd-kb01-custom:LED_SK6812MINI-ER_PLCC4_3.5x2.8mm_P1.8mm, F.Cu at (336.6, 134.1)
- added LED52: SK6812, thpd-kb01-custom:LED_SK6812MINI-ER_PLCC4_3.5x2.8mm_P1.8mm, F.Cu at (355.6, 134.1)
- added LED53: SK6812, thpd-kb01-custom:LED_SK6812MINI-ER_PLCC4_3.5x2.8mm_P1.8mm, F.Cu at (374.6, 134.1)
- added LED54: SK6812, thpd-kb01-custom:LED_SK6812MINI-ER_PLCC4_3.5x2.8mm_P1.8mm, F.Cu at (393.7, 143.7)
- added LED55: SK6812, thpd-kb01-custom:LED_SK6812MINI-ER_PLCC4_3.5x2.8mm_P1.8mm, F.Cu at (34.1, 153.2)
- added LED56: SK6812, thpd-kb01-custom:LED_SK6812MINI-ER_PLCC4_3.5x2.8mm_P1.8mm, F.Cu at (60.3, 153.2)
- added LED57: SK6812, thpd-kb01-custom:LED_SK6812MINI-ER_PLCC4_3.5x2.8mm_P1.8mm, F.Cu at (79.4, 153.2)
- added LED58: SK6812, thpd-kb01-custom:LED_SK6812MINI-ER_PLCC4_3.5x2.8mm_P1.8mm, F.Cu at (98.4, 153.2)
- added LED59: SK6812, thpd-kb01-custom:LED_SK6812MINI-ER_PLCC4_3.5x2.8mm_P1.8mm, F.Cu at (117.5, 153.2)
- added LED60: SK6812, thpd-kb01-custom:LED_SK6812MINI-ER_PLCC4_3.5x2.8mm_P1.8mm, F.Cu at (136.5, 153.2)
- added LED61: SK6812, thpd-kb01-custom:LED_SK6812MINI-ER_PLCC4_3.5x2.8mm_P1.8mm, F.Cu at (155.6, 153.2)
- added LED62: SK6812, thpd-kb01-custom:LED_SK6812MINI-ER_PLCC4_3.5x2.8mm_P1.8mm, F.Cu at (174.6, 153.2)
- added LED63: SK6812, thpd-kb01-custom:LED_SK6812MINI-ER_PLCC4_3.5x2.8mm_P1.8mm, F.Cu at (193.7, 153.2)
- added LED64: SK6812, thpd-kb01-custom:LED_SK6812MINI-ER_PLCC4_3.5x2.8mm_P1.8mm, F.Cu at (212.7, 153.2)
- added LED65: SK6812, thpd-kb01-custom:LED_SK6812MINI-ER_PLCC4_3.5x2.8mm_P1.8mm, F.Cu at (231.8, 153.2)
- added LED66: SK6812, thpd-kb01-custom:LED_SK6812MINI-ER_PLCC4_3.5x2.8mm_P1.8mm, F.Cu at (250.8, 153.2)
- added LED67: SK6812, thpd-kb01-custom:LED_SK6812MINI-ER_PLCC4_3.5x2.8mm_P1.8mm, F.Cu at (269.9, 153.2)
- added LED68: SK6812, thpd-kb01-custom:LED_SK6812MINI-ER_PLCC4_3.5x2.8mm_P1.8mm, F.Cu at (312.7, 154.0)
- added LED69: SK6812, thpd-kb01-custom:LED_SK6812MINI-ER_PLCC4_3.5x2.8mm_P1.8mm, F.Cu at (336.6, 153.2)
- added LED70: SK6812, thpd-kb01-custom:LED_SK6812MINI-ER_PLCC4_3.5x2.8mm_P1.8mm, F.Cu at (355.6, 153.2)
- added LED71: SK6812, thpd-kb01-custom:LED_SK6812MINI-ER_PLCC4_3.5x2.8mm_P1.8mm, F.Cu at (374.6, 153.2)
- added LED72: SK6812, thpd-kb01-custom:LED_SK6812MINI-ER_PLCC4_3.5x2.8mm_P1.8mm, F.Cu at (38.9, 172.2)
- added LED73: SK6812, thpd-kb01-custom:LED_SK6812MINI-ER_PLCC4_3.5x2.8mm_P1.8mm, F.Cu at (69.8, 172.2)
- added LED74: SK6812, thpd-kb01-custom:LED_SK6812MINI-ER_PLCC4_3.5x2.8mm_P1.8mm, F.Cu at (88.9, 172.2)
- added LED75: SK6812, thpd-kb01-custom:LED_SK6812MINI-ER_PLCC4_3.5x2.8mm_P1.8mm, F.Cu at (108.0, 172.2)
- added LED76: SK6812, thpd-kb01-custom:LED_SK6812MINI-ER_PLCC4_3.5x2.8mm_P1.8mm, F.Cu at (127.0, 172.2)
- added LED77: SK6812, thpd-kb01-custom:LED_SK6812MINI-ER_PLCC4_3.5x2.8mm_P1.8mm, F.Cu at (146.1, 172.2)
- added LED78: SK6812, thpd-kb01-custom:LED_SK6812MINI-ER_PLCC4_3.5x2.8mm_P1.8mm, F.Cu at (165.1, 172.2)
- added LED79: SK6812, thpd-kb01-custom:LED_SK6812MINI-ER_PLCC4_3.5x2.8mm_P1.8mm, F.Cu at (184.2, 172.2)
- added LED80: SK6812, thpd-kb01-custom:LED_SK6812MINI-ER_PLCC4_3.5x2.8mm_P1.8mm, F.Cu at (203.2, 172.2)
- added LED81: SK6812, thpd-kb01-custom:LED_SK6812MINI-ER_PLCC4_3.5x2.8mm_P1.8mm, F.Cu at (222.2, 172.2)
- added LED82: SK6812, thpd-kb01-custom:LED_SK6812MINI-ER_PLCC4_3.5x2.8mm_P1.8mm, F.Cu at (241.3, 172.2)
- added LED83: SK6812, thpd-kb01-custom:LED_SK6812MINI-ER_PLCC4_3.5x2.8mm_P1.8mm, F.Cu at (267.5, 172.2)
- added LED84: SK6812, thpd-kb01-custom:LED_SK6812MINI-ER_PLCC4_3.5x2.8mm_P1.8mm, F.Cu at (293.7, 172.2)
- added LED85: SK6812, thpd-kb01-custom:LED_SK6812MINI-ER_PLCC4_3.5x2.8mm_P1.8mm, F.Cu at (312.7, 172.2)
- added LED86: SK6812, thpd-kb01-custom:LED_SK6812MINI-ER_PLCC4_3.5x2.8mm_P1.8mm, F.Cu at (336.6, 172.2)
- added LED87: SK6812, thpd-kb01-custom:LED_SK6812MINI-ER_PLCC4_3.5x2.8mm_P1.8mm, F.Cu at (355.6, 172.2)
- added LED88: SK6812, thpd-kb01-custom:LED_SK6812MINI-ER_PLCC4_3.5x2.8mm_P1.8mm, F.Cu at (374.6, 172.2)
- added LED89: SK6812, thpd-kb01-custom:LED_SK6812MINI-ER_PLCC4_3.5x2.8mm_P1.8mm, F.Cu at (393.7, 181.8)
- added LED90: SK6812, thpd-kb01-custom:LED_SK6812MINI-ER_PLCC4_3.5x2.8mm_P1.8mm, F.Cu at (29.4, 191.3)
- added LED91: SK6812, thpd-kb01-custom:LED_SK6812MINI-ER_PLCC4_3.5x2.8mm_P1.8mm, F.Cu at (53.2, 191.3)
- added LED92: SK6812, thpd-kb01-custom:LED_SK6812MINI-ER_PLCC4_3.5x2.8mm_P1.8mm, F.Cu at (77.0, 191.3)
- added LED93: SK6812, thpd-kb01-custom:LED_SK6812MINI-ER_PLCC4_3.5x2.8mm_P1.8mm, F.Cu at (148.4, 191.3)
- added LED94: SK6812, thpd-kb01-custom:LED_SK6812MINI-ER_PLCC4_3.5x2.8mm_P1.8mm, F.Cu at (217.5, 191.3)
- added LED95: SK6812, thpd-kb01-custom:LED_SK6812MINI-ER_PLCC4_3.5x2.8mm_P1.8mm, F.Cu at (236.5, 191.3)
- added LED96: SK6812, thpd-kb01-custom:LED_SK6812MINI-ER_PLCC4_3.5x2.8mm_P1.8mm, F.Cu at (255.6, 191.3)
- added LED97: SK6812, thpd-kb01-custom:LED_SK6812MINI-ER_PLCC4_3.5x2.8mm_P1.8mm, F.Cu at (274.6, 191.3)
- added LED98: SK6812, thpd-kb01-custom:LED_SK6812MINI-ER_PLCC4_3.5x2.8mm_P1.8mm, F.Cu at (293.7, 191.3)
- added LED99: SK6812, thpd-kb01-custom:LED_SK6812MINI-ER_PLCC4_3.5x2.8mm_P1.8mm, F.Cu at (312.7, 191.3)
- C1, C10, C11, C12, C13, C14, C15, C16, C17, C18, C19, C2, C20, C21, C3, C4, C5, C6, C7, C8, C9, F1, J1, R1, R10, R2, R3, R4, R5, R6, R7, R8, R9, SW1, SW2, U1, U2, U4: moved to B.Cu
- moved D102 378.2 mm to (400.1, 83.3)
- moved D89 360.2 mm to (389.7, 169.9), turned to 270 degrees
- moved D35 358.6 mm to (389.7, 114.3), turned to 90 degrees
- moved D54 356.2 mm to (389.7, 131.8), turned to 270 degrees
- moved D71 330.8 mm to (370.7, 152.4), turned to 90 degrees
- moved R10 257.4 mm to (276.7, 119.3)
- moved R7 124.2 mm to (381.0, 89.7), turned to 180 degrees
- moved R9 123.2 mm to (384.2, 88.1), turned to 270 degrees
- moved LED10 116.3 mm to (198.4, 96.0)
- moved R6 115.2 mm to (381.0, 93.7), turned to 180 degrees
- moved C21 112.1 mm to (385.8, 83.3)
- moved R5 108.9 mm to (283.9, 148.0), turned to 270 degrees
- moved LED9 105.8 mm to (179.4, 96.0)
- moved R8 103.1 mm to (384.2, 95.2), turned to 270 degrees
- moved D101 102.6 mm to (370.7, 190.5), turned to 90 degrees
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- renumbered D101 to D100, D102 to D101, D17 to D102, D18 to D17, D19 to D18, D20 to D19, D21 to D20, D22 to D21, D23 to D22, D24 to D23, D25 to D24, D26 to D25, D27 to D26, D28 to D27, D29 to D28, D30 to D29, D31 to D30, D32 to D31, D33 to D32, D34 to D33, D35 to D34, D36 to D35, D37 to D36, D38 to D37, D39 to D38, D40 to D39, D41 to D40, D42 to D41, D43 to D42, D44 to D43, D45 to D44, D46 to D45, D47 to D46, D48 to D47, D49 to D48, D50 to D49, D51 to D50, D52 to D51, D53 to D52, D54 to D53, D55 to D54, D56 to D55, D57 to D56, D58 to D57, D59 to D58, D60 to D59, D61 to D60, D62 to D61, D63 to D62, D64 to D63, D65 to D64, D66 to D65, D67 to D66, D68 to D67, D69 to D68, D70 to D69, D71 to D70, D72 to D71, D73 to D72, D74 to D73, D75 to D74, D76 to D75, D77 to D76, D78 to D77, D79 to D78, D80 to D79, D81 to D80, D82 to D81, D83 to D82, D84 to D83, D85 to D84, D86 to D85, D87 to D86, D88 to D87, D89 to D88, D90 to D89, D91 to D90, D92 to D91, D93 to D92, D94 to D93, D95 to D94, D96 to D95, D97 to D96, D98 to D97, D99 to D98, D100 to D99, D103 to LED1, D112 to LED10, D105 to LED3, D106 to LED4, D107 to LED5, D108 to LED6, D109 to LED7, D110 to LED8, D111 to LED9
